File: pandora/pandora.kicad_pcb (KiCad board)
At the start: 2 copper layers, 121.9 x 106.7 mm, 185 parts, among them J1 SMA, J2 PinHeader_100mil_01x04, J3 JST-SH_2, J4 TX3 / MTA-156-3, J5 Conn_ARM_JTAG_SWD_10, J6 USB_B_Mini, Q1 DMP1045U, SW1 GF-126-0317, SW10 PTS645-S-H-50-SMTR92-LFS, SW11 PTS645-S-H-50-SMTR92-LFS, SW12 PTS645-S-H-50-SMTR92-LFS, SW13 PTS645-S-M-43-SMTR92-LFS, SW14 PTS645-S-K-50-SMTR92-LFS, SW15 PTS645-S-K-50-SMTR92-LFS, SW16 PTS645-S-K-50-SMTR92-LFS, SW17 PTS645-S-K-50-SMTR92-LFS, SW18 PTS526-S-K-15-SMTR92-LFS, SW2 PTS645-S-H-50-SMTR92-LFS, SW3 PTS645-S-H-50-SMTR92-LFS, SW4 PTS645-S-H-50-SMTR92-LFS, SW5 PTS645-S-H-50-SMTR92-LFS, SW6 PTS645-S-H-50-SMTR92-LFS, SW7 PTS645-S-H-50-SMTR92-LFS, SW8 PTS645-S-H-50-SMTR92-LFS, SW9 PTS645-S-M-43-SMTR92-LFS, U1 LM1086CS-ADJ, U10 ADM811ZARTZ, U11 LCD_Adafruit_16x02_Neg_RGB, U12 MCP73831-2-OT, U13 MCP1642D-50, U2 MCP1702T-3302, U3 MCP1702T-3302, U4 MCP6001, U5 MPU-9250, U6 ULN2003D, U7 74LCX245, U8 CC2652R, U9 74LVC1G08, Y1 NC26_32.768k, Y2 FA-238_48M

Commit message: Move things around
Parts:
- moved G*** 1.14 mm to (112.1, 143.0)
- moved J6 0.76 mm to (133.5, 140.0)
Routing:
- net Net-(F1-Pad1): track 4.36 -> 5.13 mm
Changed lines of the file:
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@@
   (general
     (thickness 1.6)
-    (drawings 151)
+    (drawings 158)
     (tracks 1898)
     (zones 0)
@@
     (nets 134)
   )
-  (page A4)
+  (page USLetter)
   (title_block
     (title "Pandora CC2652R Development Board")
@@
   )
   (module pandora:logo-caltech-ee (layer B.Cu)
-    (at 111.125 143.51 180)
+    (at 112.141 143.002 180)
     (fp_text reference G*** (at 0 0) (layer B.SilkS) hide
       (effects (font (size 1.524 1.524) (thickness 0.3)) (justify mirror))
@@
   )
   (module pandora:USB_MiniB_KMBSMT5SS30 (layer F.Cu)
-    (at 133.477 139.192)
+    (at 133.477 139.954)
     (descr "USB Mini-B receptacle, SMD pads, locator pegs")
     (tags "USB Mini-B")
@@
     )
   )
+  (gr_line (start 194.437 42.672) (end 199.009 42.672) (layer B.SilkS) (width 0.762))
+  (gr_line (start 190.119 42.672) (end 190.627 42.672) (layer B.SilkS) (width 0.762))
+  (gr_line (start 185.801 42.672) (end 186.309 42.672) (layer B.SilkS) (width 0.762))
+  (gr_line (start 86.995 42.672) (end 181.737 42.672) (layer B.SilkS) (width 0.762))
+  (gr_line (start 203.073 46.99) (end 203.073 143.51) (layer B.SilkS) (width 0.762))
+  (gr_line (start 82.677 46.99) (end 82.677 143.51) (layer B.SilkS) (width 0.762))
+  (gr_line (start 86.995 147.828) (end 199.009 147.828) (layer B.SilkS) (width 0.762))
   (gr_circle (center 140.335 97.79) (end 144.399 97.79) (layer B.SilkS) (width 1.27))
   (gr_circle (center 140.335 97.79) (end 144.399 97.79) (layer F.SilkS) (width 1.27))
@@
   (segment (start 134.112 135.89) (end 133.35 136.652) (width 0.762) (layer F.Cu) (net 38))
   (segment (start 133.477 137.287) (end 133.35 137.16) (width 0.508) (layer F.Cu) (net 38))
-  (segment (start 133.477 138.992102) (end 133.477 137.287) (width 0.508) (layer F.Cu) (net 38))
+  (segment (start 133.477 139.754102) (end 133.477 137.287) (width 0.508) (layer F.Cu) (net 38))
   (segment (start 156.150001 132.865001) (end 151.476401 128.191401) (width 1.27) (layer F.Cu) (net 39))
   (segment (start 156.150001 135.822501) (end 156.150001 132.865001) (width 1.27) (layer F.Cu) (net 39))

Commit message: Continue decorating
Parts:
- added G***: LOGO, pandora:logo-srh, B.Cu at (148.0, 142.5)
- added G***: LOGO, pandora:logo-srh, F.Cu at (134.0, 61.7)
- added H7: #6, pandora:MountingHole_No6, F.Cu at (198.8, 97.8)
- SW18: value PTS526-S-K-15-SMTR92-LFS -> PTS526-S-K-15-SMTR92
- moved G*** 0.80 mm to (147.7, 84.1)
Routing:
- net GNDRF: vias 158 -> 2
- net GNDBAT: vias 46 -> 57
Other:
- board text added: "NO ADDITIONAL COPPER"

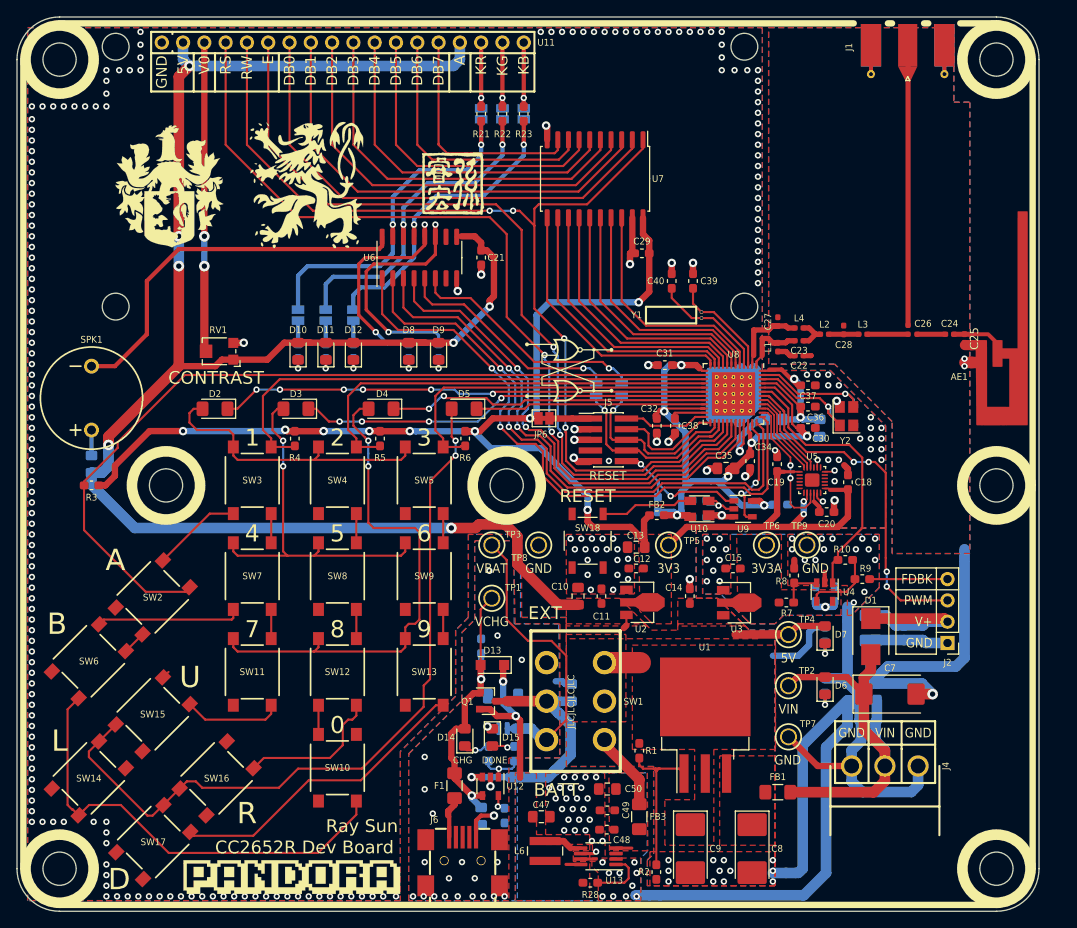
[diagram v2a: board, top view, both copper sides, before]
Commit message: Re-make RF section
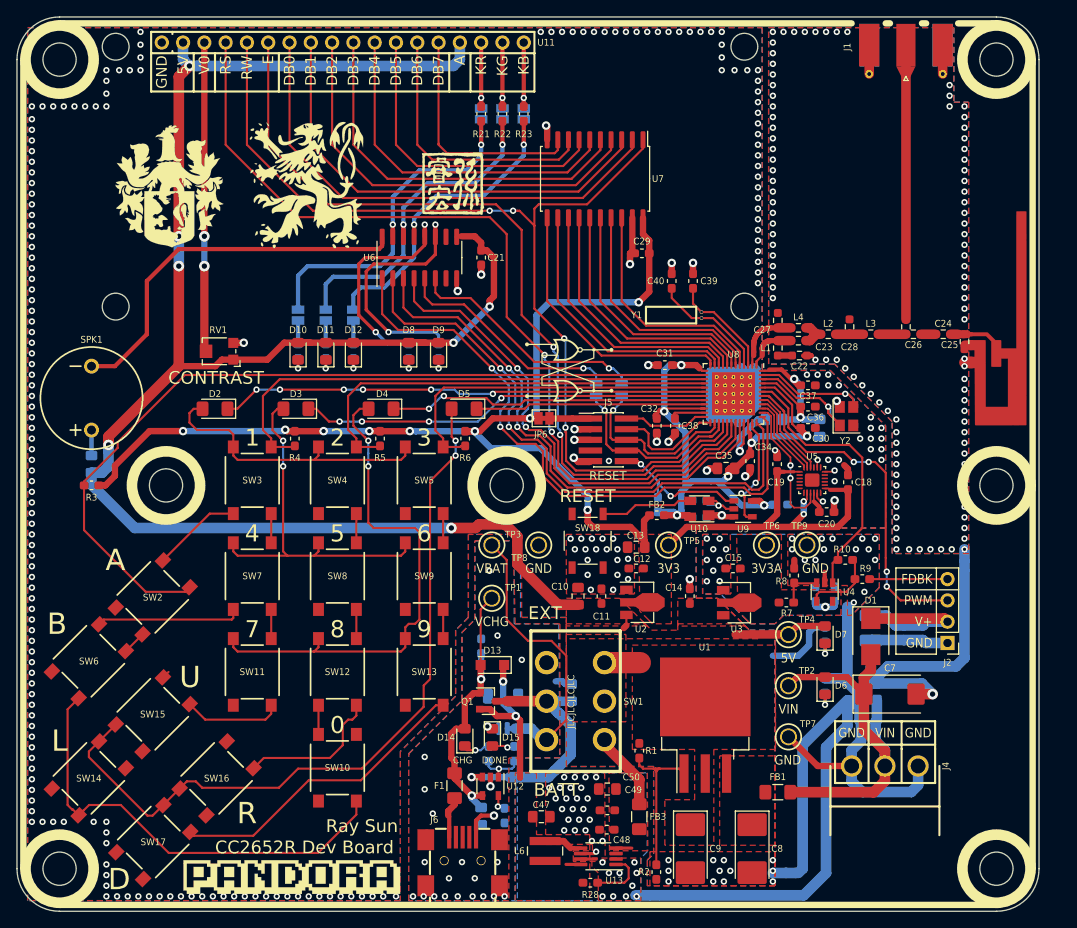
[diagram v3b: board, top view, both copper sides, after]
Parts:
- C22, C23, C24, C25, C27, C28, L1, L2, L3, L4: footprint pandora:0402_HandSoldering -> pandora:0603
- C26: footprint pandora:0402_Branch_HandSoldering -> pandora:0603_Branch
- moved L3 0.95 mm to (183.8, 79.8)
- moved C28 0.79 mm to (181.2, 78.9)
- moved C24 0.76 mm to (192.4, 79.8)
- moved L2 0.44 mm to (178.7, 79.8)
- moved C25 0.38 mm to (194.9, 80.6)
- moved C26 0.25 mm to (188.0, 79.8)
- moved J1 0.21 mm to (188.0, 47.0)
- moved AE1 0.15 mm to (199.0, 79.8)
- moved C27 0.14 mm to (172.7, 78.1)
- moved L1 0.11 mm to (172.7, 81.4)
- moved C23 0.08 mm to (175.1, 80.5)
- moved L4 0.08 mm to (175.1, 79.0)
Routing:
- net GNDRF: track 4.63 -> 11.5 mm, vias 2 -> 103
- net Net-(C26-Pad3): track 37.5 -> 32.8 mm
- net /mcu/RF_N: track 9.93 -> 8.26 mm
- net Net-(C24-Pad2): track 3.37 -> 1.78 mm
- net Net-(C26-Pad1): track 4.81 -> 3.30 mm
- net /mcu/RF_P: track 7.64 -> 6.19 mm
- net Net-(C22-Pad2): track 2.22 -> 1.69 mm
- added copper zone on F.Cu, net Net-(AE1-Pad1)
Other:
- net class CPWG: trace_width 0.6096 -> 1.143

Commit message: Stitch RF plane and decorate
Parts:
- removed the G*** at (148.0, 142.5)
- added G***: LOGO, pandora:logo-srh-large, B.Cu at (183.3, 65.0)
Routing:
- net GNDRF: vias 103 -> 139

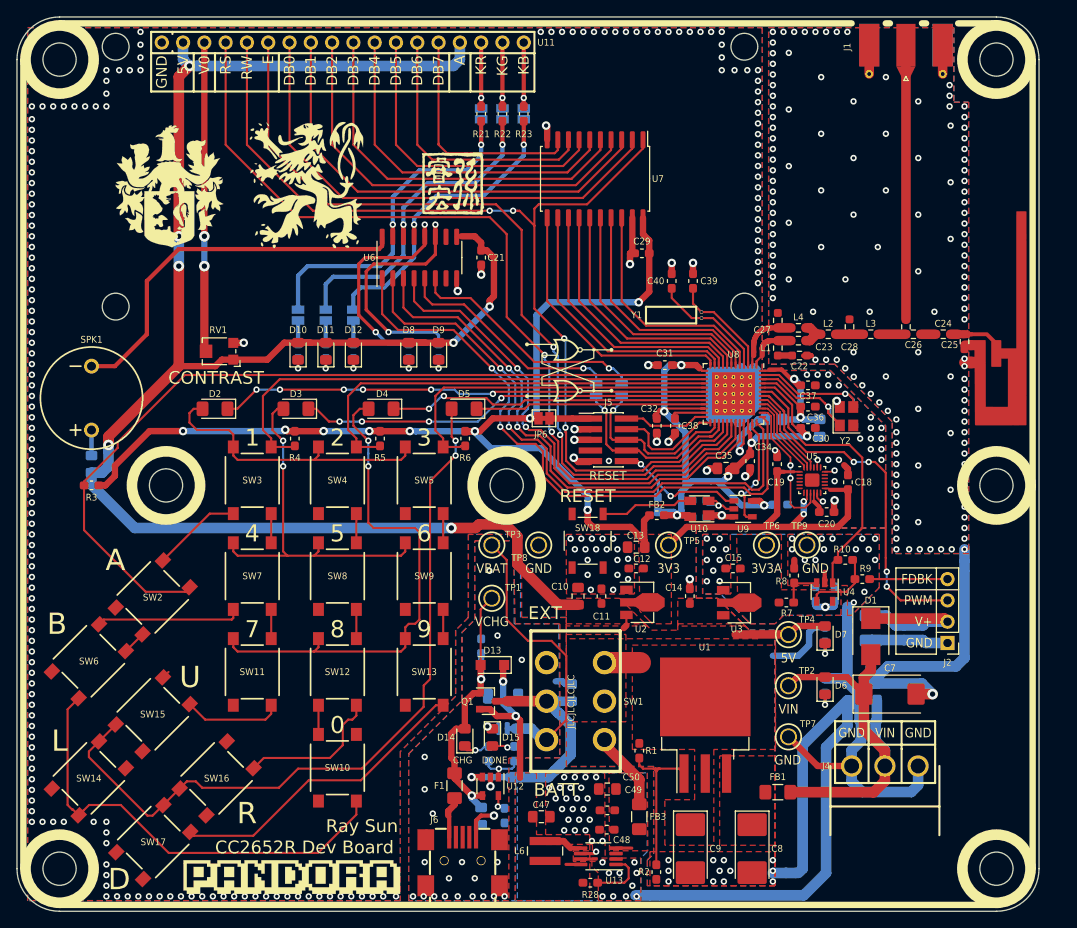
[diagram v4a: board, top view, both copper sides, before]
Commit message: Fix planes
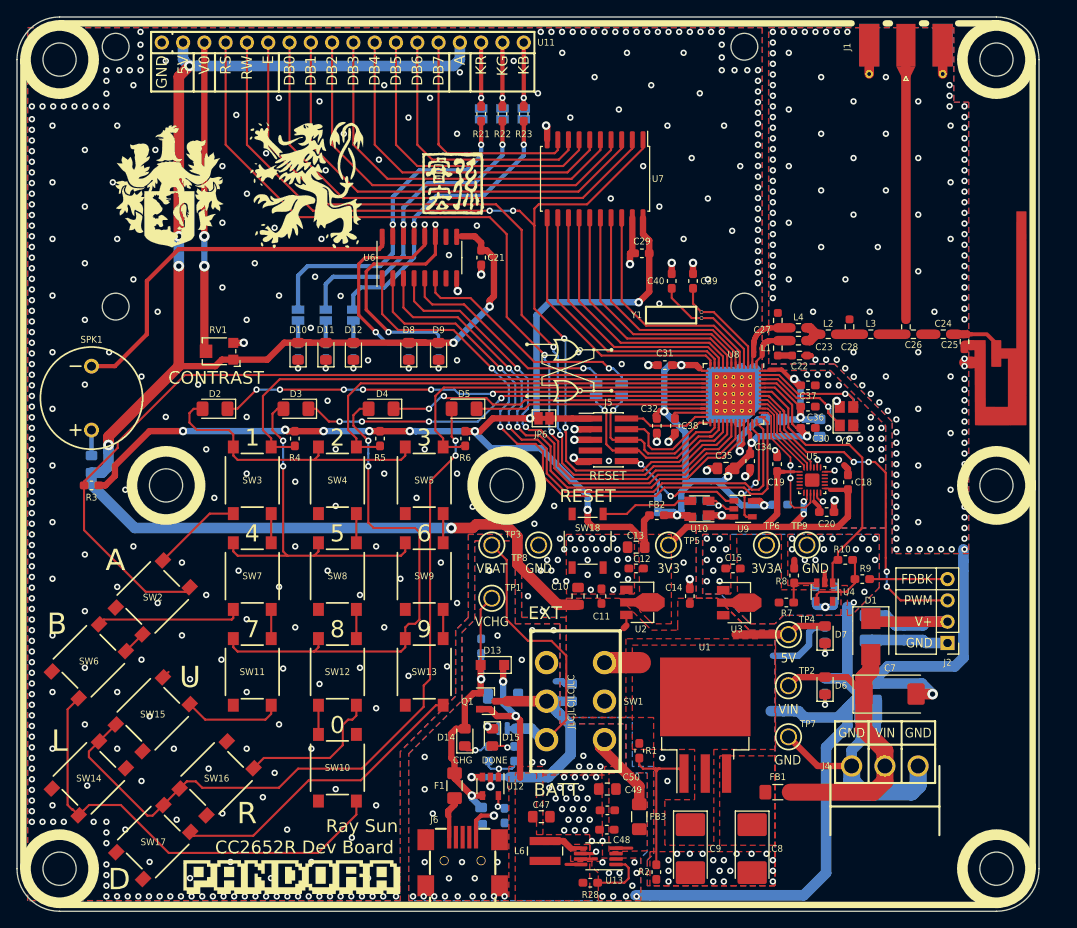
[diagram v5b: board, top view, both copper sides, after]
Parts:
- moved NT1 19.3 mm to (174.0, 124.7)
- moved NT3 0.13 mm to (194.8, 107.4)
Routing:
- net GNDIN: track 145.8 -> 130.6 mm
- net GNDD: track 72.4 -> 72.3 mm, vias 237 -> 416
- net GNDBAT: vias 57 -> 65

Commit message: Regenerate project output
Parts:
- moved C15 2.54 mm to (169.9, 107.7)
- moved C16 2.54 mm to (182.0, 110.8)
- moved C17 2.54 mm to (179.7, 110.8)
- moved C19 2.54 mm to (175.1, 95.2)
- moved C22 2.54 mm to (177.8, 82.3)
- moved C25 2.54 mm to (197.5, 80.6)
- moved C32 2.54 mm to (160.8, 90.7)
- moved C34 2.54 mm to (171.9, 94.9)
- moved C44 2.54 mm to (175.5, 100.1)
- moved C46 2.54 mm to (150.6, 122.5)
- moved C5 2.54 mm to (190.2, 115.4)
- moved C6 2.54 mm to (192.5, 115.4)
- moved C8 2.54 mm to (172.2, 141.1)
- moved D13 2.54 mm to (141.2, 119.2)
- moved D14 2.54 mm to (137.9, 127.8)
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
